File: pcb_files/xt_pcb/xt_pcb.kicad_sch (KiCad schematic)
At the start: 31 parts, among them J1 Conn_01x04_Socket, J2 Conn_01x05, U1 XC6206PxxxMR, U2 RP2040, U3 W25Q128JVS, Y1 Crystal_GND24

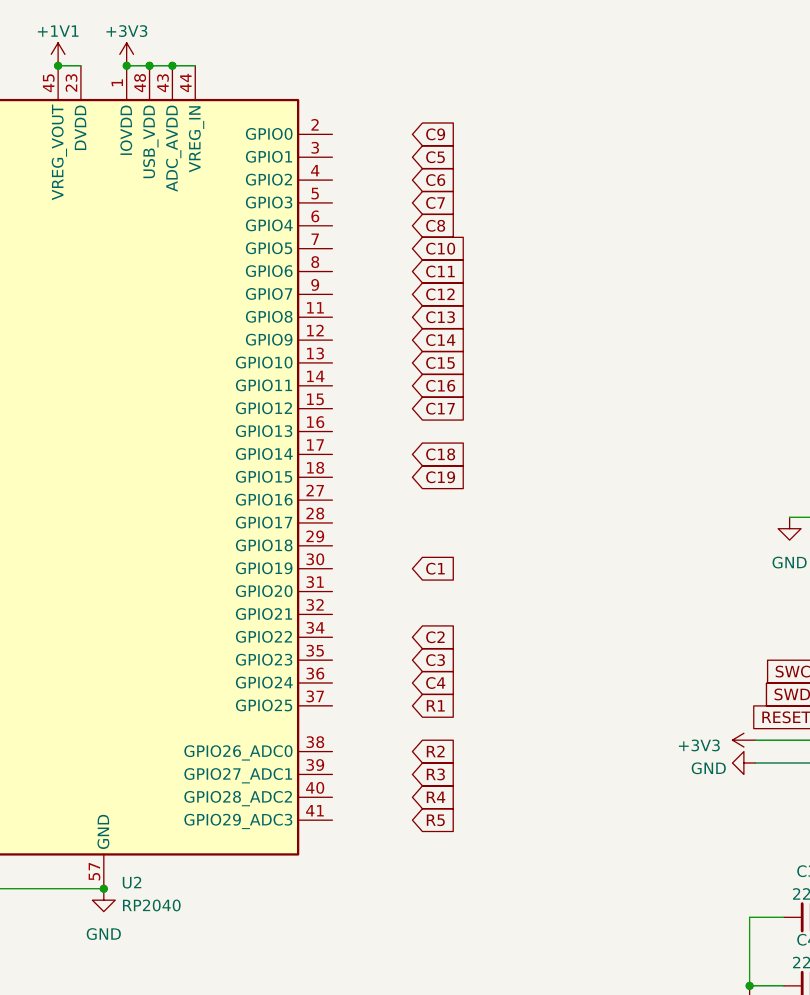
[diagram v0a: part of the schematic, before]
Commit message: connected connected the switch matrix to gpio
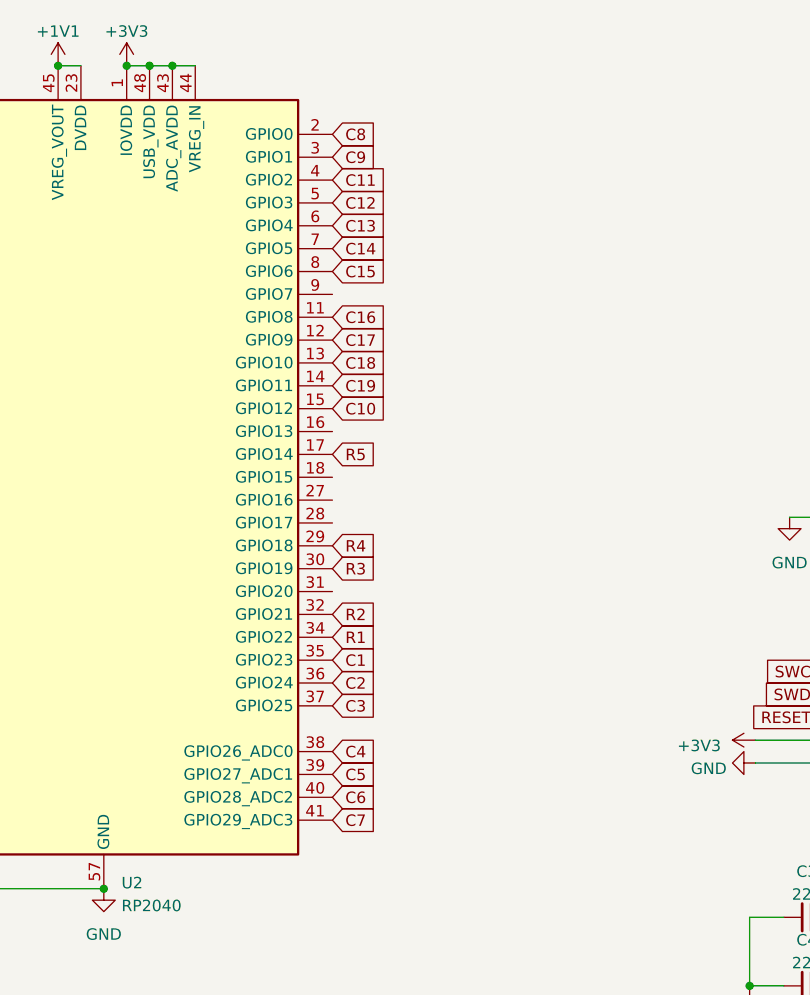
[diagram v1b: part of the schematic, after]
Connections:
- net C1: now also U2.35 (GPIO23)
- net C10: now also U2.15 (GPIO12)
- net C11: now also U2.4 (GPIO2)
- net C12: now also U2.5 (GPIO3)
- net C13: now also U2.6 (GPIO4)
- net C14: now also U2.7 (GPIO5)
- net C15: now also U2.8 (GPIO6)
- net C16: now also U2.11 (GPIO8)
- net C17: now also U2.12 (GPIO9)
- net C18: now also U2.13 (GPIO10)
- net C19: now also U2.14 (GPIO11)
- net C2: now also U2.36 (GPIO24)
- net C3: now also U2.37 (GPIO25)
- net C4: now also U2.38 (GPIO26_ADC0)
- net C5: now also U2.39 (GPIO27_ADC1)
- net C6: now also U2.40 (GPIO28_ADC2)
- net C7: now also U2.41 (GPIO29_ADC3)
- net C8: now also U2.2 (GPIO0)
- net C9: now also U2.3 (GPIO1)
- net R1: now also U2.34 (GPIO22)
- net R2: now also U2.32 (GPIO21)
- net R3: now also U2.30 (GPIO19)
- net R4: now also U2.29 (GPIO18)
- net R5: now also U2.17 (GPIO14)
